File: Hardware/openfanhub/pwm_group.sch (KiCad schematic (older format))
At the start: 3 parts, among them J7 Conn_01x04_Male, J8 Conn_01x04_Male, J9 Conn_01x04_Male

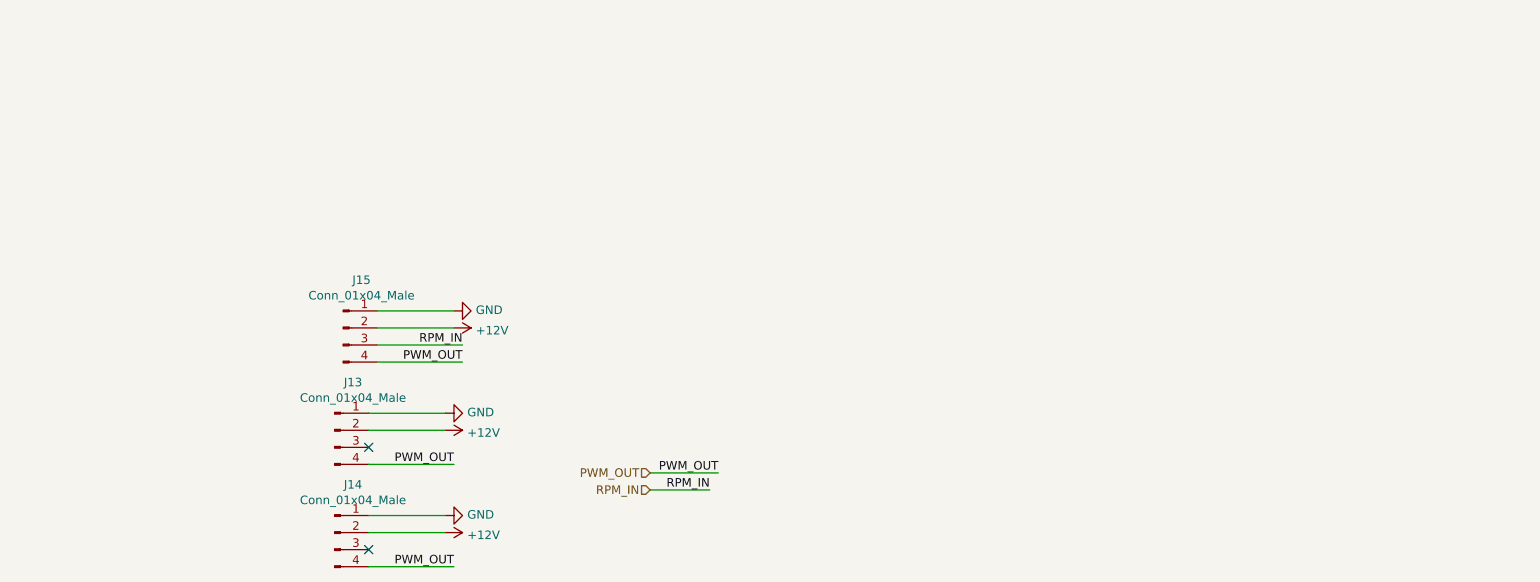
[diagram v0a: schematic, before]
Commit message: Update schematics with new pin layout
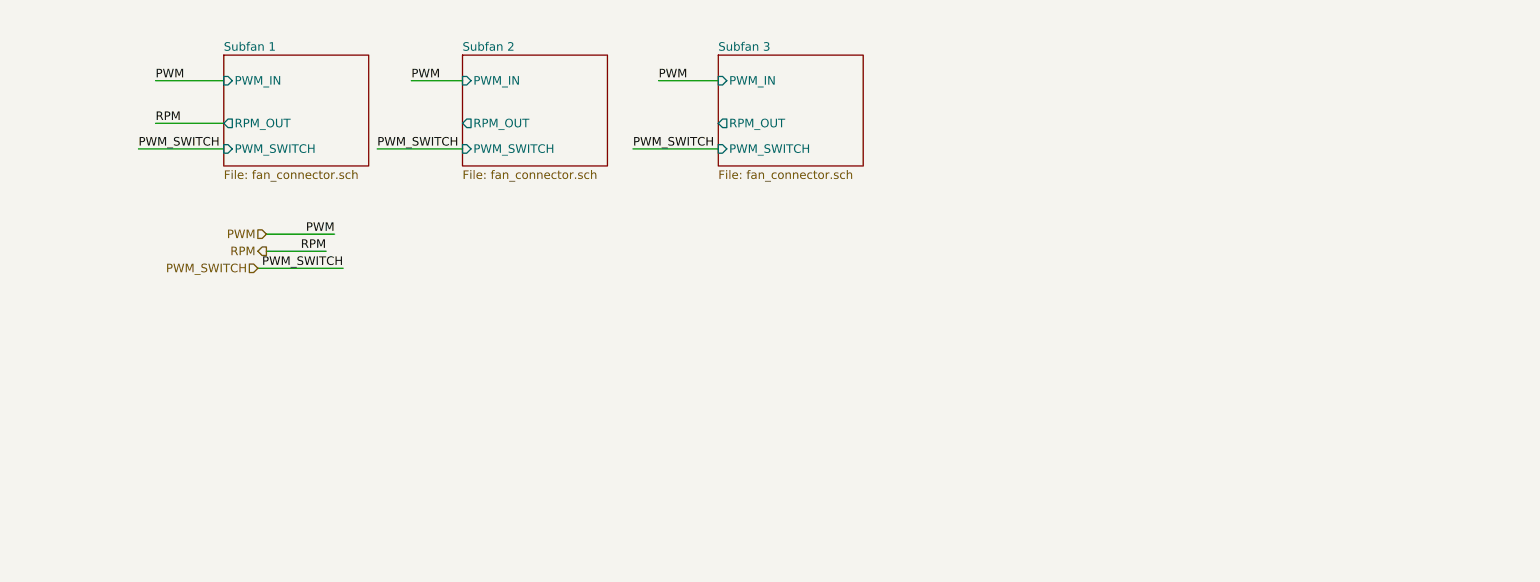
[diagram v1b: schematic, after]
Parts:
- removed J7, J8, J9: Conn_01x04_Male, Connector_PinHeader_2.54mm:PinHeader_1x04_P2.54mm_Horizontal, symbol Connector:Conn_01x04_Male
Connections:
- no-connect marks 2 -> 0

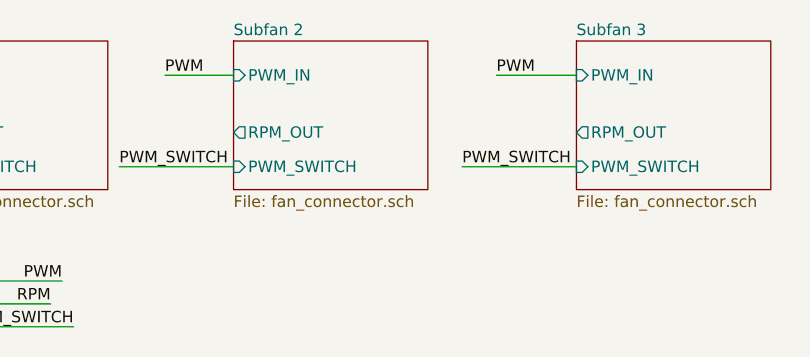
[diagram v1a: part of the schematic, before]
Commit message: Enable fan by default (even if µC is offline)
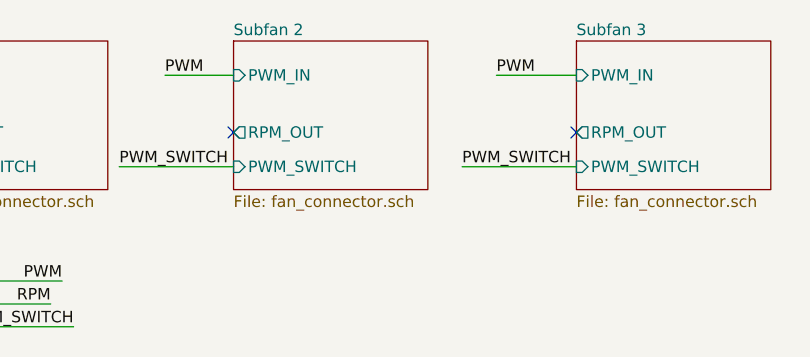
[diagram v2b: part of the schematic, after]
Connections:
- no-connect marks 0 -> 2
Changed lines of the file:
@@
 Wire Wire Line
 	2550 2250 2050 2250
+NoConn ~ 3250 1400
+NoConn ~ 4750 1400
 $EndSCHEMATC

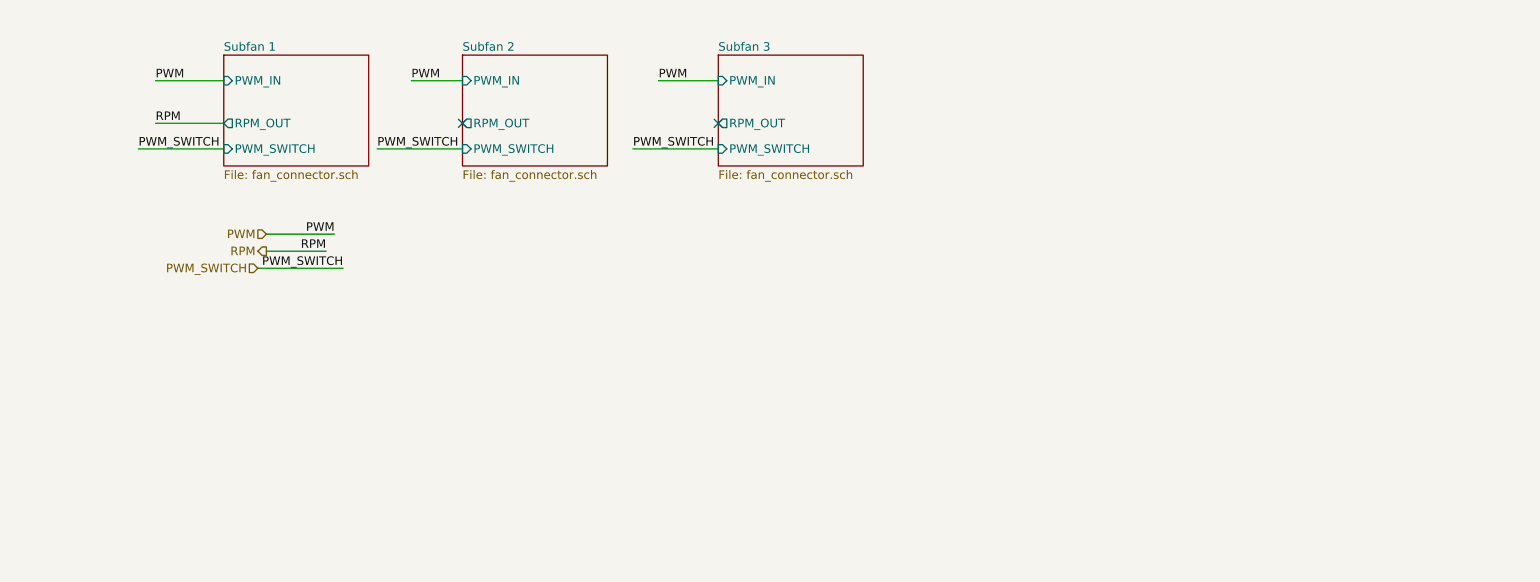
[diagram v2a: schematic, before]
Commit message: Update files to kicad 6
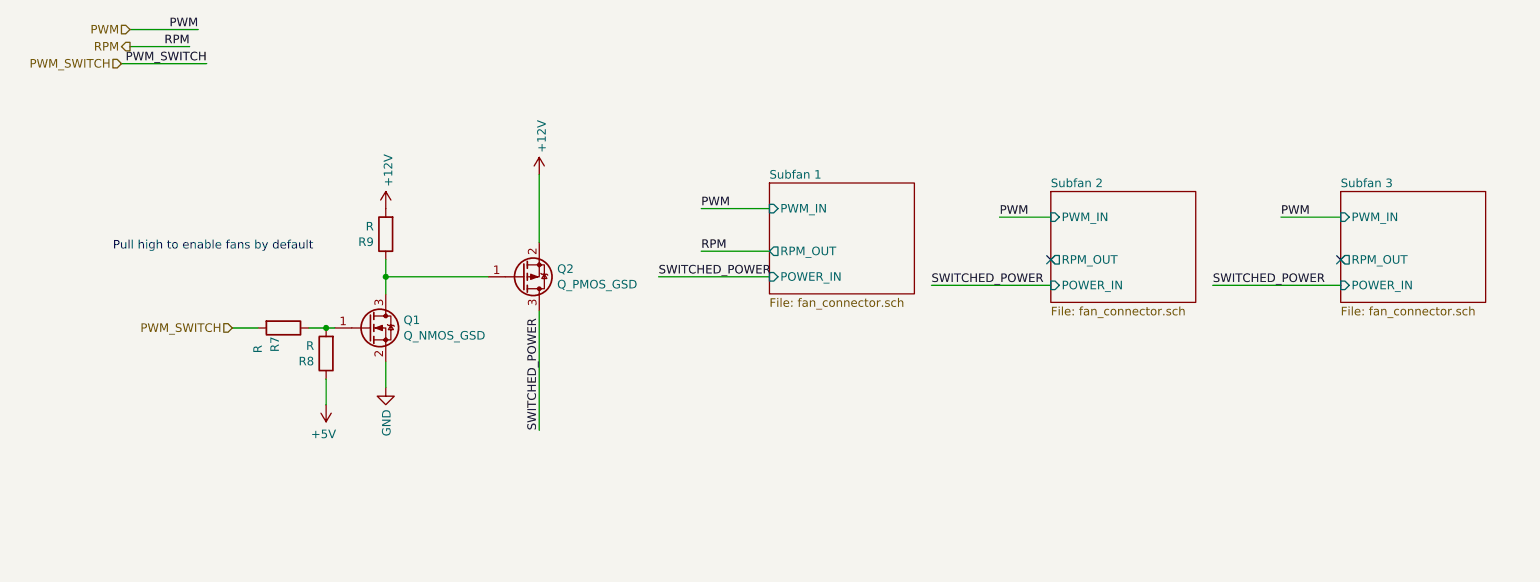
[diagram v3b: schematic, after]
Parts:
- added Q1: Q_NMOS_GSD, Package_TO_SOT_SMD:SOT-23, symbol Device:Q_NMOS_GSD
- added Q2: Q_PMOS_GSD, Package_TO_SOT_SMD:SOT-23, symbol Device:Q_PMOS_GSD
- added R7, R8, R9: R, Resistor_SMD:R_0805_2012Metric, symbol Device:R
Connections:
- net PWM_SWITCH: now also R7.2
- new net: Q1.3 (D), Q2.1 (G), R9.1
- new net: Q1.1 (G), R7.1, R8.2
- new net +12V: Q2.2 (S), R9.2
- new net +5V: R8.1
- new net GND: Q1.2 (S)
- new net SWITCHED_POWER: Q2.3 (D)
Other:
- note added: "Pull high to enable fans by default\n"
